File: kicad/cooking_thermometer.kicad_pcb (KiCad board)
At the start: 2 copper layers, 60.5 x 40.4 mm, 53 parts, among them J1 FTDI, J2 STLINK, J3 3V3_Power, J4 Battery, J6 OLED_CONN, J8 THERMO_CONN, J9 USB_C, Q1 BC547, SW1 BOOT0_SW, SW2 NRST_SW, SW3 UI_A_SW, SW4 UI_B_SW, SW5 UI_C_SW, U1 STM32G0B0KETx, U2 MCP1700x-330xxTO, U3 MCP73831-2-OT

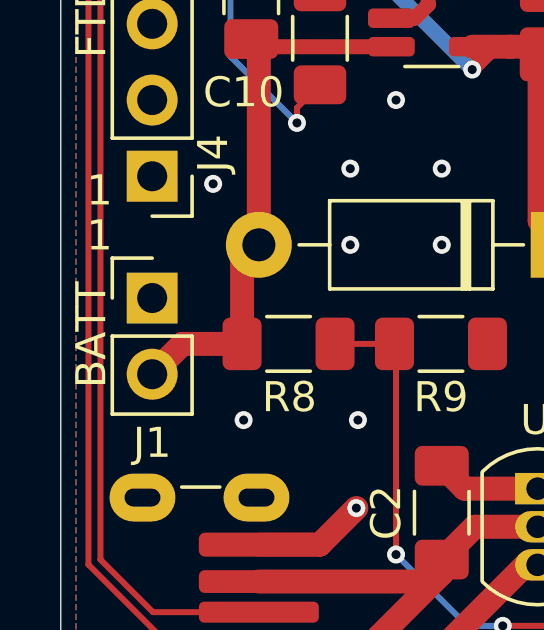
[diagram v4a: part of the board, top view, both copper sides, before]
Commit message: Add +- to battery connection
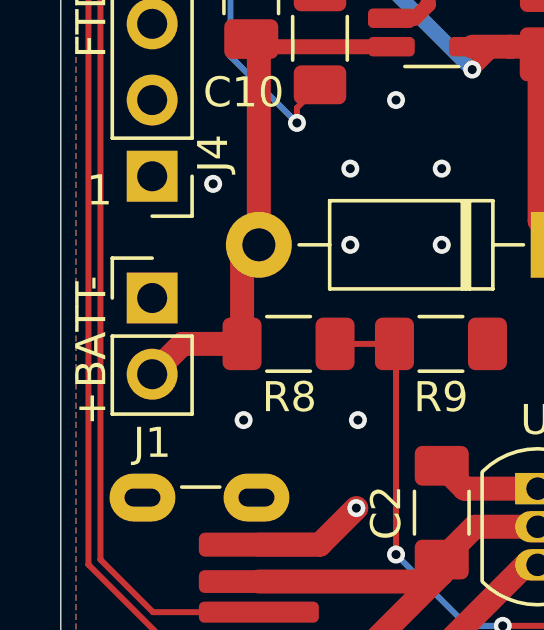
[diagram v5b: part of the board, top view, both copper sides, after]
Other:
- board text added: "+"
- board text added: "-"
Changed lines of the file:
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@@
-		)
-	)
-	(gr_text "1"
-		(at 153 94 0)
-		(layer "F.SilkS")
-		(effects
-			(font
-				(size 1 1)
-				(thickness 0.1)
-			)
-			(justify left bottom)
 		)
 	)
@@
 		)
 	)
+	(gr_text "+"
+		(at 153.75 99.75 90)
+		(layer "F.SilkS")
+		(effects
+			(font
+				(size 1 1)
+				(thickness 0.1)
+			)
+			(justify left bottom)
+		)
+	)
 	(gr_text "1"
 		(at 167 78 0)
 		(layer "F.SilkS")
 		(effects
+			(font
+				(size 1 1)
+				(thickness 0.1)
+			)
+			(justify left bottom)
+		)
+	)
+	(gr_text "-"
+		(at 153.75 95.25 90)
+		(layer "F.SilkS")
+		(effects

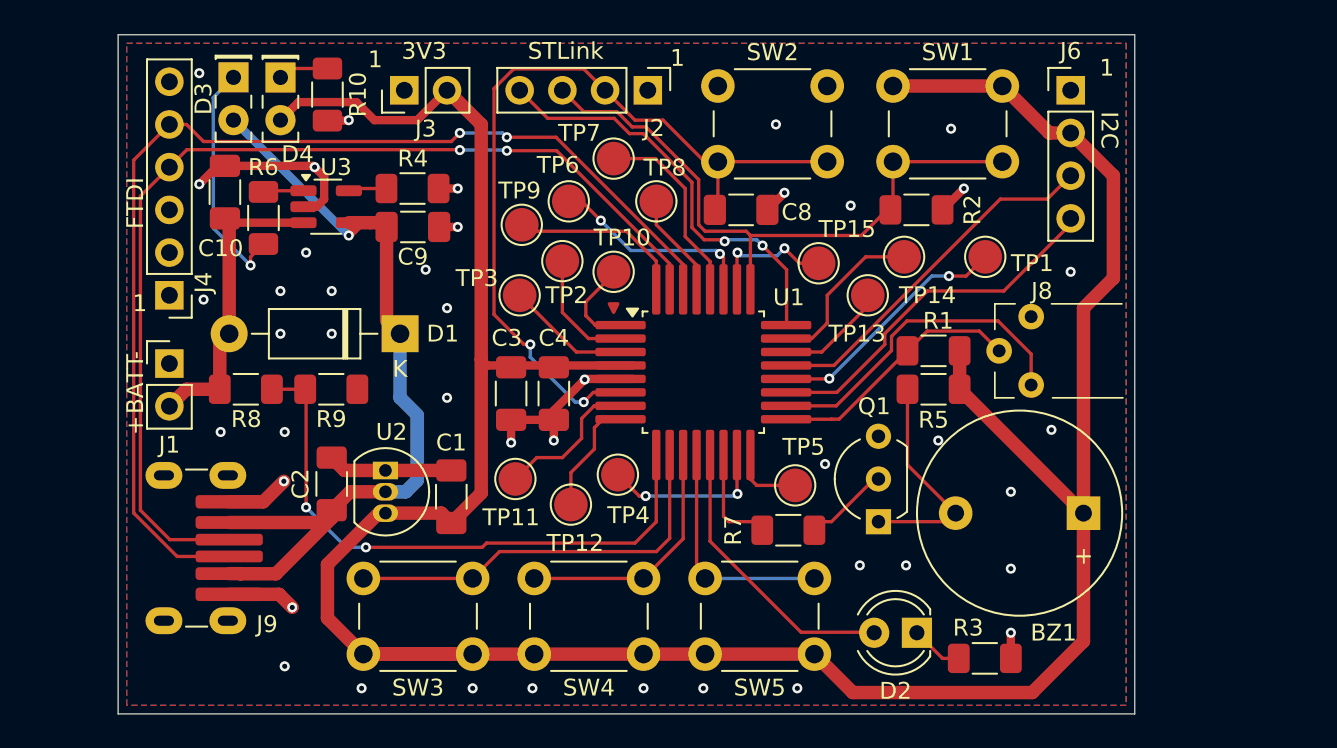
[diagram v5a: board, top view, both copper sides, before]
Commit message: Change 2.5mm jack, make the board bigger, add mounting holes. Some rewiring.
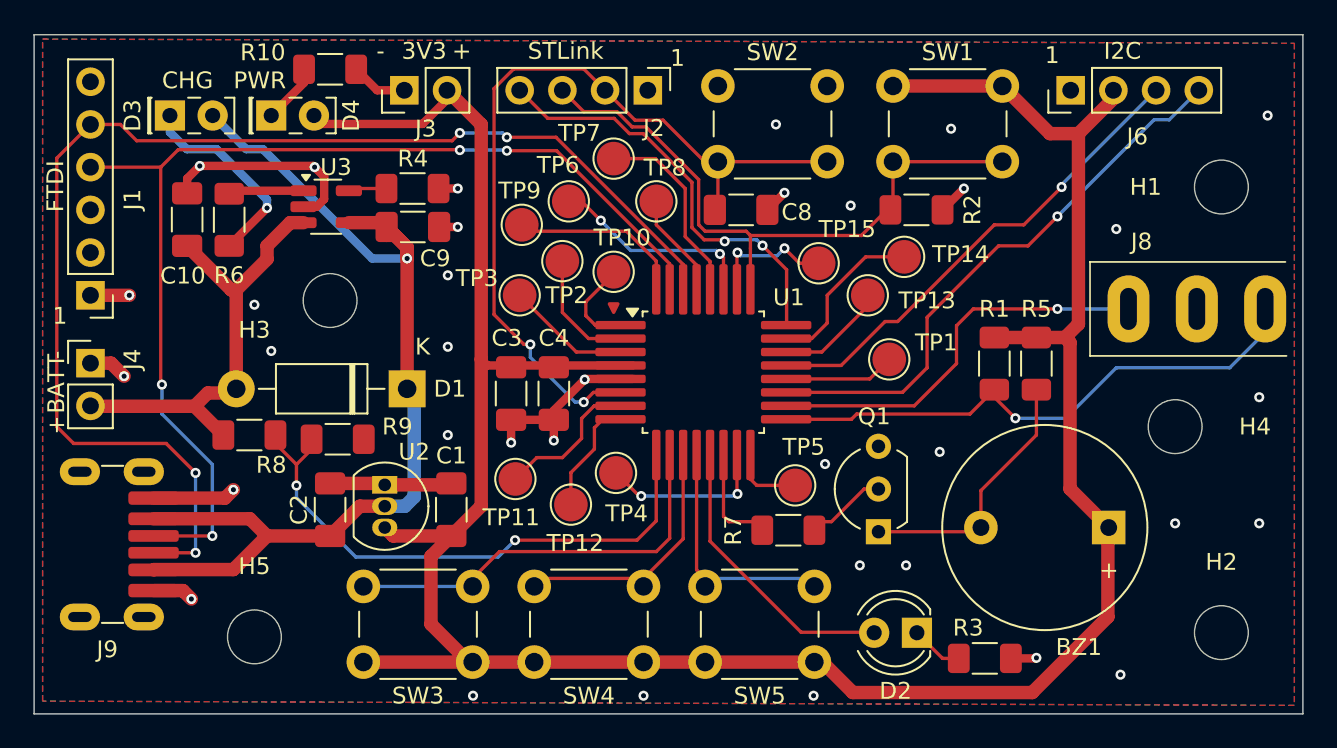
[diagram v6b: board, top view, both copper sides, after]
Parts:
- added H1: MountingHole, MountingHole:MountingHole_3.2mm_M3, F.Cu at (217.8, 85.0)
- added H2: MountingHole, MountingHole:MountingHole_3.2mm_M3, F.Cu at (217.8, 111.5)
- added H3: MountingHole, MountingHole:MountingHole_3.2mm_M3, F.Cu at (164.8, 91.8)
- added H4: MountingHole, MountingHole:MountingHole_3.2mm_M3, F.Cu at (215.0, 99.2)
- added H5: MountingHole, MountingHole:MountingHole_3.2mm_M3, F.Cu at (160.2, 111.8)
- J8: footprint MyOwnFootprintLibrary:AudioJack_Mono_2.5mm_with_Tip-Detect -> MyOwnFootprintLibrary:Jack_Mono_2.5mm_with_Tip-Detect_Electrokit_41010270
- J9: footprint MyOwnFootprintLibrary:USB_C_Receptacle_GCT_USB4125-xx-x_6P_TopMnt_Horizontal_Long_Pads -> MyOwnFootprintLibrary:USB_C_Receptacle_6P_TopMnt_Horizontal_Long_Pads_Electrokit_41021035
- moved J8 10.0 mm to (214.3, 94.8)
- moved TP1 8.35 mm to (198.0, 95.2)
- moved R5 6.30 mm to (206.8, 95.5), turned to -90 degrees
- moved J9 5.00 mm to (150.7, 106.2)
- moved J4 4.69 mm to (150.5, 95.5)
- moved J1 4.69 mm to (150.5, 91.4)
- moved D3 4.41 mm to (155.2, 80.8), turned to 0 degrees
- moved R1 3.69 mm to (204.2, 95.5), turned to -90 degrees
- moved D1 3.30 mm to (169.3, 97.0)
- moved R9 3.00 mm to (165.2, 100.0)
- moved C10 2.78 mm to (156.2, 86.9)
- moved R8 2.73 mm to (159.9, 99.8)
- moved D4 2.33 mm to (161.2, 80.8), turned to 0 degrees
- moved R6 2.04 mm to (158.8, 87.0)
- moved BZ1 1.73 mm to (211.1, 105.2)
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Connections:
- net /~{JACK_CONNECTED} renamed /JACK_CONNECTED
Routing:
- net /ADC10_TEMP_MEAS: track 16.1 -> 33.7 mm, vias 0 -> 1
- net +3.3V: track 171.1 -> 156.3 mm
- net +5V_USB: track 49.7 -> 62.0 mm
- net /I2C1_SCL: track 22.5 -> 34.5 mm, vias 0 -> 1
- net /UART1_TX: track 67.4 -> 76.7 mm, vias 2 -> 4
- net +BATT: track 18.3 -> 27.5 mm
- net Net-(U1-PC6): track 14.8 -> 6.61 mm, vias 2 -> 0
- net GND: track 45.6 -> 53.2 mm, vias 43 -> 35
- net /I2C1_SDA: track 22.3 -> 29.6 mm, vias 0 -> 1
- net /UART1 RX: track 62.4 -> 66.7 mm, vias 2 -> 4
- net /JACK_CONNECTED: track 20.6 -> 24.1 mm, vias 0 -> 1
- net /ADC2_BATT_MEAS: track 36.2 -> 33.8 mm
- net Net-(BZ1--): track 13.6 -> 15.8 mm
- net Net-(U3-STAT): track 2.41 -> 4.49 mm
- net Net-(D3-K): track 14.2 -> 12.1 mm
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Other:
- board size 60.5 x 40.4 mm -> 75.5 x 40.4 mm
- board text added: "CHG"
- board text added: "PWR"

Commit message: Add extra series on pullup NTC. Move stuff around.
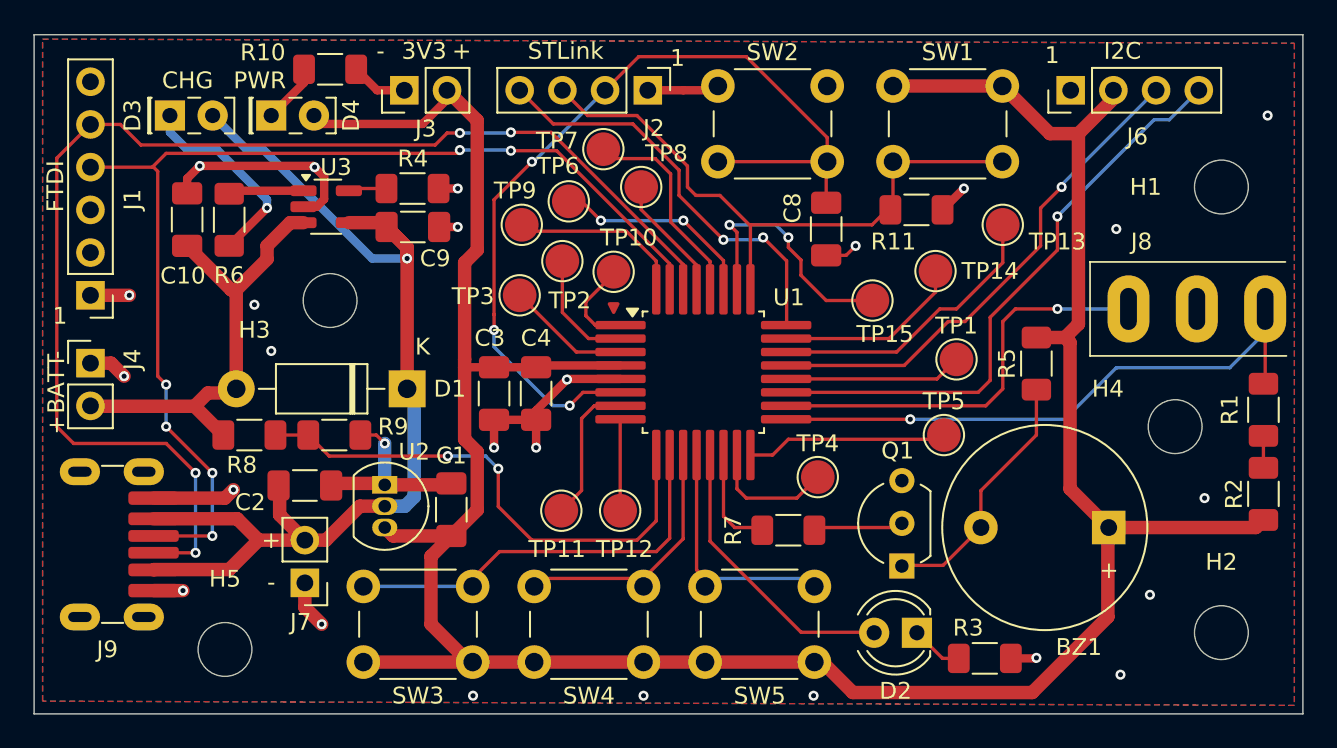
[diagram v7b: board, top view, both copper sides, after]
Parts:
- added J7: 5V_Power, Connector_PinHeader_2.54mm:PinHeader_1x02_P2.54mm_Vertical, F.Cu at (163.2, 108.5)
- added R2: 100k, Resistor_SMD:R_1206_3216Metric_Pad1.30x1.75mm_HandSolder, F.Cu at (220.2, 103.2)
- R1: value 200k -> 100k
- moved R1 16.2 mm to (220.2, 98.2), turned to 90 degrees
- moved TP4 12.0 mm to (193.8, 102.2)
- moved TP5 9.34 mm to (201.2, 99.8)
- moved TP13 9.05 mm to (204.8, 87.2)
- moved C8 5.19 mm to (194.2, 87.5), turned to 90 degrees
- moved TP1 4.00 mm to (202.0, 95.2)
- moved TP15 3.89 mm to (197.0, 91.8)
- moved TP11 3.32 mm to (178.5, 104.2)
- moved TP12 2.95 mm to (182.0, 104.2)
- moved Q1 2.47 mm to (198.8, 107.5)
- moved C2 2.08 mm to (163.2, 102.8), turned to 0 degrees
- moved TP14 2.05 mm to (200.8, 90.0)
- moved H5 1.90 mm to (158.5, 112.5)
- moved TP8 1.24 mm to (183.2, 85.0)
- moved C4 1.05 mm to (177.0, 97.3)
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- renumbered R2 to R11
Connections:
- R1 pad 1: +3.3V -> Net-(R1-Pad1)
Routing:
- net GND: track 53.2 -> 65.3 mm, vias 35 -> 26
- net Net-(U1-PA11/PA9): track 7.37 -> 18.1 mm
- net Net-(U1-PB1): track 4.25 -> 12.0 mm
- net Net-(U1-PA15): track 7.65 -> 15.3 mm
- net +3.3V: track 156.3 -> 163.7 mm
- net /NRST: track 50.1 -> 54.5 mm, vias 2 -> 3
- net Net-(U1-PC6): track 6.61 -> 10.6 mm
- net +5V_USB: track 62.0 -> 65.5 mm
- net /ADC2_BATT_MEAS: track 33.8 -> 30.9 mm
- net /ADC10_TEMP_MEAS: track 33.7 -> 36.5 mm
- net Net-(U1-PB0): track 10.0 -> 7.56 mm, vias 2 -> 0
- net Net-(R1-Pad1): track 0.00 -> 1.90 mm
- net /I2C1_SCL: track 34.5 -> 36.1 mm
- net Net-(U1-PA1): track 6.92 -> 5.46 mm
- net /I2C1_SDA: track 29.6 -> 30.9 mm
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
